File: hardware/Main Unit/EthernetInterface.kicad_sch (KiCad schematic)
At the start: 22 parts, among them J13 HFJ11-2450E-L21RL, U7 KSZ8081RND

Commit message: Main unit: Add USB port for MCU and 3.3VA rail, start on routing
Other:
- moved on the sheet: FB1
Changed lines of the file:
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@@
 	)
 	(junction
+		(at 133.35 33.02)
+		(diameter 0)
+		(color 0 0 0 0)
+	)
+	(junction
 		(at 92.71 48.26)
 		(diameter 0)
@@
 	)
 	(junction
+		(at 200.66 90.17)
+		(diameter 0)
+		(color 0 0 0 0)
+	)
+	(junction
 		(at 165.1 39.37)
 		(diameter 0)
@@
 	(wire
 		(pts
+			(xy 133.35 33.02) (xy 127 33.02)
+		)
+		(stroke
+			(width 0)
+			(type default)
+		)
+	)
+	(wire
+		(pts
 			(xy 139.7 66.04) (xy 170.18 66.04)
 		)
@@
 	(wire
 		(pts
-			(xy 148.59 33.02) (xy 140.97 33.02)
+			(xy 156.21 33.02) (xy 148.59 33.02)
 		)
 		(stroke
@@
 	(wire
 		(pts
-			(xy 200.66 78.74) (xy 200.66 91.44)
+			(xy 200.66 78.74) (xy 200.66 90.17)
 		)
 		(stroke
@@
 	(wire
 		(pts
-			(xy 148.59 30.48) (xy 148.59 33.02)
+			(xy 156.21 30.48) (xy 156.21 33.02)
 		)
 		(stroke
@@
 	(wire
 		(pts
-			(xy 135.89 33.02) (xy 127 33.02)
+			(xy 143.51 33.02) (xy 133.35 33.02)
 		)
 		(stroke
@@
 	(wire
 		(pts
+			(xy 200.66 90.17) (xy 200.66 91.44)
+		)
+		(stroke
+			(width 0)
+			(type default)
+		)
+	)
+	(wire
+		(pts
 			(xy 137.16 87.63) (xy 137.16 85.09)
 		)
@@
 	)
 	(symbol
+		(lib_id "power:PWR_FLAG")
+		(at 133.35 33.02 0)
+		(unit 1)
+		(exclude_from_sim no)
+		(in_bom yes)
+		(on_board yes)
+		(dnp no)
+		(fields_autoplaced yes)
+		(property "Reference" "#FLG02"
+			(at 133.35 31.115 0)
+			(effects
+				(font
+					(size 1.27 1.27)
+				)
+				(hide yes)
+			)
+		)
+		(property "Value" "PWR_FLAG"
+			(at 133.35 27.94 0)
+			(effects
+				(font
+					(size 1.27 1.27)
+				)
+			)
+		)
+		(property "Footprint" ""
+			(at 133.35 33.02 0)
+			(effects
+				(font
+					(size 1.27 1.27)
+				)
+				(hide yes)
+			)
+		)
+		(property "Datasheet" "~"
+			(at 133.35 33.02 0)
+			(effects
+				(font
+					(size 1.27 1.27)
+				)
+				(hide yes)
+			)
+		)
+		(property "Description" "Special symbol for telling ERC where power comes from"
+			(at 133.35 33.02 0)
+			(effects
+				(font
+					(size 1.27 1.27)
+				)
+				(hide yes)
+			)
+		)
+		(pin "1"
+		)
+		(instances
+			(project ""
+				(path "/7d91f165-331a-4c48-9d02-ee2a0aa7e94a/f20a5acb-4894-4073-8c07-952a30c65f74"
+					(reference "#FLG02")
+					(unit 1)
+				)
+			)
+		)
+	)
+	(symbol
 		(lib_id "Device:R_Small_US")
 		(at 81.28 69.85 90)
@@
 	(symbol
 		(lib_id "power:+8V")
-		(at 148.59 30.48 0)
+		(at 156.21 30.48 0)
 		(unit 1)
 		(exclude_from_sim no)
@@
 		(dnp no)
 		(property "Reference" "#PWR0118"
-			(at 148.59 34.29 0)
+			(at 156.21 34.29 0)
 			(effects
 				(font
@@
 		)
 		(property "Value" "+3.3V"
-			(at 152.146 29.718 0)
+			(at 159.766 29.718 0)
 			(effects
 				(font
@@
 		)
 		(property "Footprint" ""
-			(at 148.59 30.48 0)
+			(at 156.21 30.48 0)
 			(effects
 				(font
@@
 		)
 		(property "Datasheet" ""
-			(at 148.59 30.48 0)
+			(at 156.21 30.48 0)
 			(effects
 				(font
@@
 		)
 		(property "Description" "Power symbol creates a global label with name \"+8V\""
-			(at 148.59 30.48 0)
+			(at 156.21 30.48 0)
 			(effects
 				(font
@@
 	(symbol
 		(lib_id "Device:FerriteBead_Small")
-		(at 138.43 33.02 90)
+		(at 146.05 33.02 90)
 		(unit 1)
 		(exclude_from_sim no)
@@
 		(dnp no)
 		(property "Reference" "FB1"
-			(at 140.97 27.94 90)
+			(at 148.59 27.94 90)
 			(effects
 				(font
@@
 		)
 		(property "Value" "300@100MHz"
-			(at 138.43 30.48 90)
+			(at 146.05 30.48 90)
 			(effects
 				(font
@@
 		)
 		(property "Footprint" "Resistor_SMD:R_1206_3216Metric"
-			(at 138.43 34.798 90)
+			(at 146.05 34.798 90)
 			(effects
 				(font
@@
 		)
 		(property "Datasheet" "~"
-			(at 138.43 33.02 0)
+			(at 146.05 33.02 0)
 			(effects
 				(font
@@
 		)
 		(property "Description" "Ferrite bead, small symbol"
-			(at 138.43 33.02 0)
+			(at 146.05 33.02 0)
 			(effects
 				(font
@@
 		)
 		(property "SKU" "732-4654-1-ND"
-			(at 138.43 33.02 0)
+			(at 146.05 33.02 0)
 			(effects
 				(font
@@
 		)
 		(property "Supplier" "Digi-Key"
-			(at 138.43 33.02 0)
+			(at 146.05 33.02 0)
 			(effects
 				(font
@@
 		)
 		(property "LibRef" "742792121"
-			(at 138.43 33.02 0)
+			(at 146.05 33.02 0)
 			(effects
 				(font
@@
 					(unit 1)
 				)
+			)
+		)
+	)
+	(symbol
+		(lib_id "power:PWR_FLAG")
+		(at 200.66 90.17 90)
+		(unit 1)
+		(exclude_from_sim no)
+		(in_bom yes)
+		(on_board yes)
+		(dnp no)
+		(fields_autoplaced yes)
+		(property "Reference" "#FLG03"
+			(at 198.755 90.17 0)
+			(effects
+				(font
+					(size 1.27 1.27)
+				)
+				(hide yes)
+			)
+		)
+		(property "Value" "PWR_FLAG"
+			(at 196.85 90.1699 90)
+			(effects
+				(font
+					(size 1.27 1.27)
+				)
+				(justify left)
+			)
+		)
+		(property "Footprint" ""
+			(at 200.66 90.17 0)
+			(effects
+				(font
+					(size 1.27 1.27)
+				)
+				(hide yes)
+			)
+		)
+		(property "Datasheet" "~"
+			(at 200.66 90.17 0)
+			(effects
+				(font
+					(size 1.27 1.27)
+				)
+				(hide yes)
+			)
+		)
+		(property "Description" "Special symbol for telling ERC where power comes from"
+			(at 200.66 90.17 0)
+			(effects
+				(font
+					(size 1.27 1.27)
+				)
+				(hide yes)
+			)
+		)
+		(pin "1"
+		)
+		(instances
+			(project ""
+				(path "/7d91f165-331a-4c48-9d02-ee2a0aa7e94a/f20a5acb-4894-4073-8c07-952a30c65f74"
+					(reference "#FLG03")
+					(unit 1)
+				)

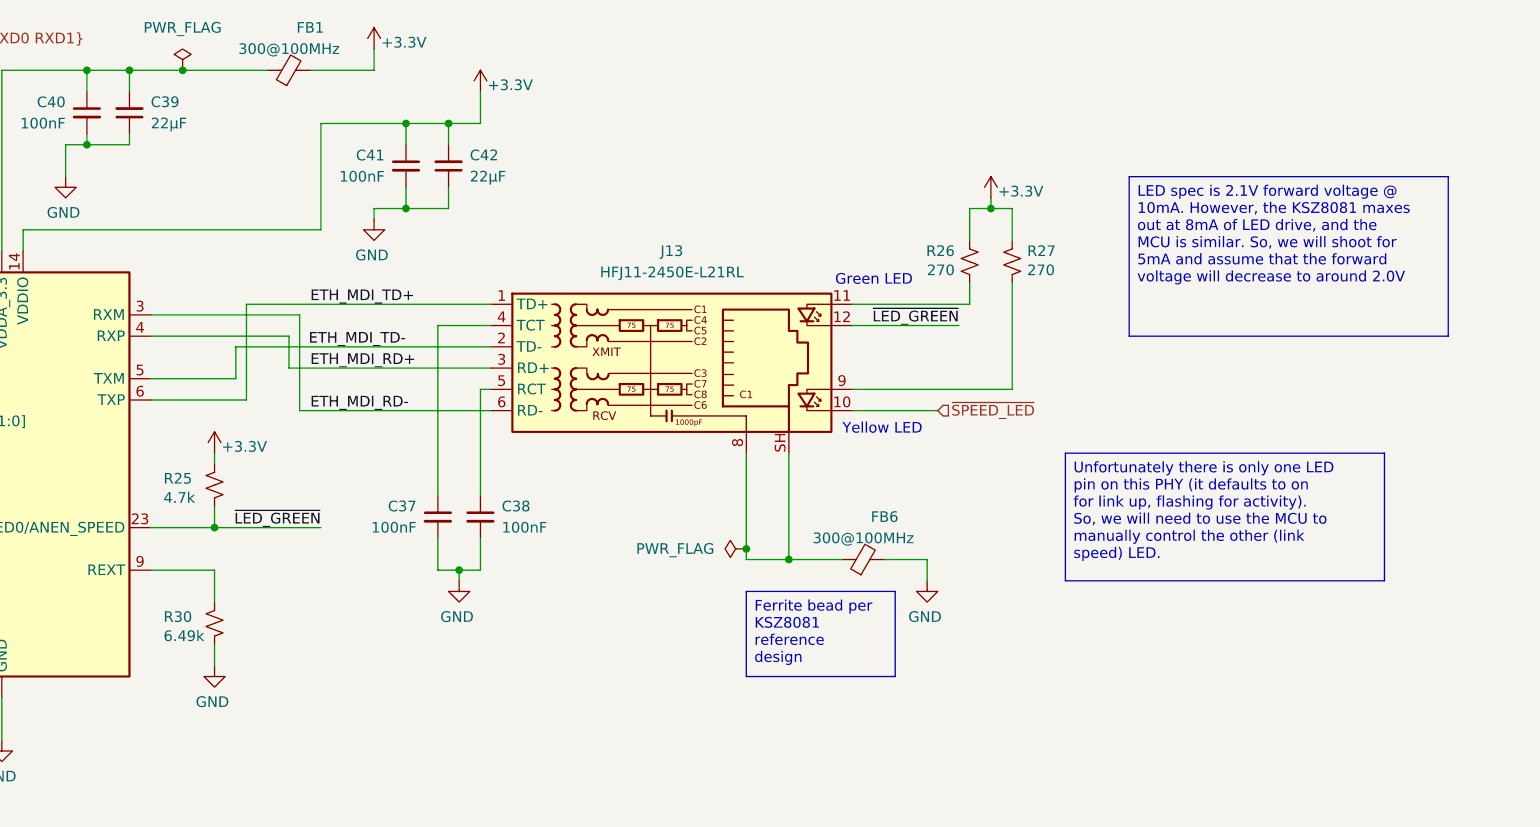
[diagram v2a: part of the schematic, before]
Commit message: Route most of the data lines on the PCB
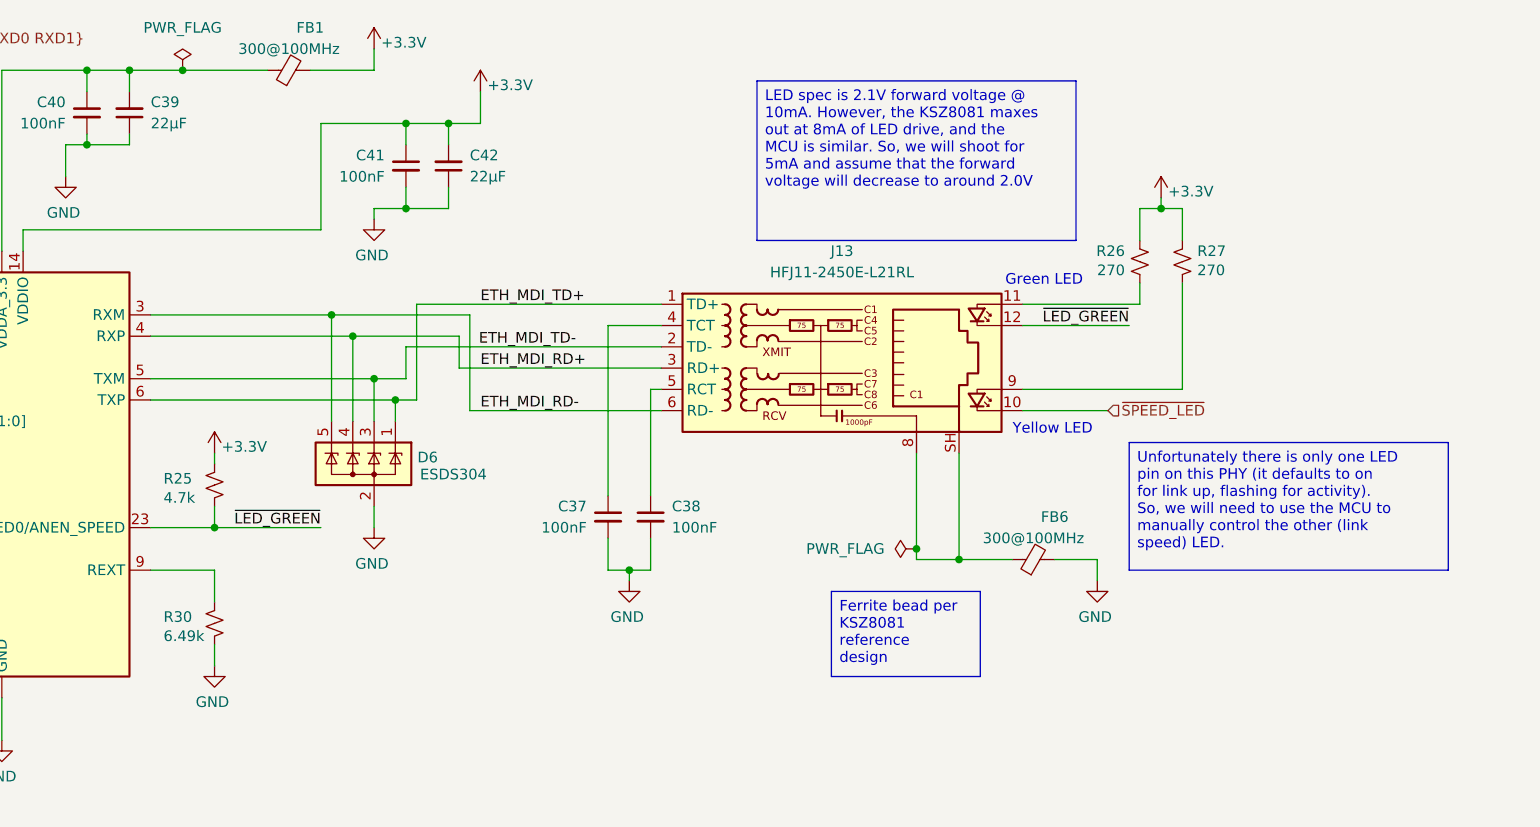
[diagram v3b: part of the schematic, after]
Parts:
- added D6: ESDS304, Package_TO_SOT_SMD:SOT-23-5, symbol Power_Protection:ESDS304
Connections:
- net ETH_MDI_RD+: now also D6.4 (K)
- net ETH_MDI_RD-: now also D6.5 (K)
- net ETH_MDI_TD+: now also D6.1 (K)
- net ETH_MDI_TD-: now also D6.3 (K)
- net GND: now also D6.2 (A)
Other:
- moved on the sheet: C37, C38, FB6, J13, R26, R27

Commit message: Add LEDs and 5V regulator to main unit
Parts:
- J13: footprint Project Library:RJ45_HALO_HFJ11-x2450E-LxxRL_Horizontal-Fixed3DModel -> Connector_RJ:RJ45_HALO_HFJ11-x2450E-LxxRL_Horizontal
- U7: footprint Project Library:QFN-24-1EP_4x4mm_P0.5mm_EP2.65x2.65mm-LengthenedPads -> Package_DFN_QFN:QFN-24-1EP_4x4mm_P0.5mm_EP2.6x2.6mm
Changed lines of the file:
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@@
 		)
 		(instances
-			(project "Main Unit"
+			(project "HackerDAQ Main Unit"
 				(path "/7d91f165-331a-4c48-9d02-ee2a0aa7e94a/f20a5acb-4894-4073-8c07-952a30c65f74"
 					(reference "#PWR0145")
@@
 		)
 		(instances
-			(project ""
+			(project "HackerDAQ Main Unit"
 				(path "/7d91f165-331a-4c48-9d02-ee2a0aa7e94a/f20a5acb-4894-4073-8c07-952a30c65f74"
 					(reference "#FLG02")
@@
 			)
 		)
-		(property "Description" "Resistor 33 ohm 1% 0.1W 0603"
+		(property "Description" "Resistor, small US symbol"
 			(at 81.28 69.85 0)
 			(effects
@@
 		)
 		(instances
-			(project "Main Unit"
+			(project "HackerDAQ Main Unit"
 				(path "/7d91f165-331a-4c48-9d02-ee2a0aa7e94a/f20a5acb-4894-4073-8c07-952a30c65f74"
 					(reference "R13")
@@
 		)
 		(instances
-			(project "Main Unit"
+			(project "HackerDAQ Main Unit"
 				(path "/7d91f165-331a-4c48-9d02-ee2a0aa7e94a/f20a5acb-4894-4073-8c07-952a30c65f74"
 					(reference "#PWR089")
@@
 			)
 		)
-		(property "Description" "CAP CER 22uF 16V X7R 1210"
+		(property "Description" "Unpolarized capacitor, small symbol"
 			(at 127 38.1 0)
 			(effects
@@
 		)
 		(instances
-			(project "Main Unit"
+			(project "HackerDAQ Main Unit"
 				(path "/7d91f165-331a-4c48-9d02-ee2a0aa7e94a/f20a5acb-4894-4073-8c07-952a30c65f74"
 					(reference "C39")
@@
 		)
 		(instances
-			(project "Main Unit"
+			(project "HackerDAQ Main Unit"
 				(path "/7d91f165-331a-4c48-9d02-ee2a0aa7e94a/f20a5acb-4894-4073-8c07-952a30c65f74"
 					(reference "C38")
@@
 			)
 		)
-		(property "Description" "CAP CER 22uF 16V X7R 1210"
+		(property "Description" "Unpolarized capacitor, small symbol"
 			(at 165.1 44.45 0)
 			(effects
@@
 		)
 		(instances
-			(project "Main Unit"
+			(project "HackerDAQ Main Unit"
 				(path "/7d91f165-331a-4c48-9d02-ee2a0aa7e94a/f20a5acb-4894-4073-8c07-952a30c65f74"
 					(reference "C42")
@@
 			)
 		)
-		(property "Description" "Resistor 6.49 kOhm 1% 0.1W 0603"
+		(property "Description" "Resistor, small US symbol"
 			(at 137.16 99.06 0)
 			(effects
@@
 		)
 		(instances
-			(project "Main Unit"
+			(project "HackerDAQ Main Unit"
 				(path "/7d91f165-331a-4c48-9d02-ee2a0aa7e94a/f20a5acb-4894-4073-8c07-952a30c65f74"
 					(reference "R30")
@@
 		)
 		(instances
-			(project "Main Unit"
+			(project "HackerDAQ Main Unit"
 				(path "/7d91f165-331a-4c48-9d02-ee2a0aa7e94a/f20a5acb-4894-4073-8c07-952a30c65f74"
 					(reference "C37")
@@
 		)
 		(instances
-			(project "Main Unit"
+			(project "HackerDAQ Main Unit"
 				(path "/7d91f165-331a-4c48-9d02-ee2a0aa7e94a/f20a5acb-4894-4073-8c07-952a30c65f74"
 					(reference "#PWR0118")
@@
 			)
 		)
-		(property "Footprint" "Project Library:QFN-24-1EP_4x4mm_P0.5mm_EP2.65x2.65mm-LengthenedPads"
+		(property "Footprint" "Package_DFN_QFN:QFN-24-1EP_4x4mm_P0.5mm_EP2.6x2.6mm"
 			(at 147.32 107.95 0)
 			(effects
@@
 		)
 		(instances
-			(project ""
+			(project "HackerDAQ Main Unit"
 				(path "/7d91f165-331a-4c48-9d02-ee2a0aa7e94a/f20a5acb-4894-4073-8c07-952a30c65f74"
 					(reference "U7")
@@
 		)
 		(instances
-			(project "Main Unit"
+			(project "HackerDAQ Main Unit"
 				(path "/7d91f165-331a-4c48-9d02-ee2a0aa7e94a/f20a5acb-4894-4073-8c07-952a30c65f74"
 					(reference "C40")
@@
 		)
 		(instances
-			(project "Main Unit"
+			(project "HackerDAQ Main Unit"
 				(path "/7d91f165-331a-4c48-9d02-ee2a0aa7e94a/f20a5acb-4894-4073-8c07-952a30c65f74"
 					(reference "#PWR0116")
@@
 		)
 		(instances
-			(project "Main Unit"
+			(project "HackerDAQ Main Unit"
 				(path "/7d91f165-331a-4c48-9d02-ee2a0aa7e94a/f20a5acb-4894-4073-8c07-952a30c65f74"
 					(reference "#PWR088")
@@
 		)
 		(instances
-			(project "Main Unit"
+			(project "HackerDAQ Main Unit"
 				(path "/7d91f165-331a-4c48-9d02-ee2a0aa7e94a/f20a5acb-4894-4073-8c07-952a30c65f74"
 					(reference "FB1")
@@
 		)
 		(instances
-			(project "Main Unit"
+			(project "HackerDAQ Main Unit"
 				(path "/7d91f165-331a-4c48-9d02-ee2a0aa7e94a/f20a5acb-4894-4073-8c07-952a30c65f74"
 					(reference "C35")
@@
 		)
 		(instances
-			(project ""
+			(project "HackerDAQ Main Unit"
 				(path "/7d91f165-331a-4c48-9d02-ee2a0aa7e94a/f20a5acb-4894-4073-8c07-952a30c65f74"
 					(reference "D6")
@@
 		)
 		(instances
-			(project "Main Unit"
+			(project "HackerDAQ Main Unit"
 				(path "/7d91f165-331a-4c48-9d02-ee2a0aa7e94a/f20a5acb-4894-4073-8c07-952a30c65f74"
 					(reference "C41")
@@
 		)
 		(instances
-			(project "Main Unit"
+			(project "HackerDAQ Main Unit"
 				(path "/7d91f165-331a-4c48-9d02-ee2a0aa7e94a/f20a5acb-4894-4073-8c07-952a30c65f74"
 					(reference "#PWR0114")
@@
 			)
 		)
-		(property "Description" "Resistor 33 ohm 1% 0.1W 0603"
+		(property "Description" "Resistor, small US symbol"
 			(at 81.28 74.93 0)
 			(effects
@@
 		)
 		(instances
-			(project "Main Unit"
+			(project "HackerDAQ Main Unit"
 				(path "/7d91f165-331a-4c48-9d02-ee2a0aa7e94a/f20a5acb-4894-4073-8c07-952a30c65f74"
 					(reference "R16")
@@
 			)
 		)
-		(property "Description" "Resistor 33 ohm 1% 0.1W 0603"
+		(property "Description" "Resistor, small US symbol"
 			(at 72.39 80.01 0)
 			(effects
@@
 		)
 		(instances
-			(project "Main Unit"
+			(project "HackerDAQ Main Unit"
 				(path "/7d91f165-331a-4c48-9d02-ee2a0aa7e94a/f20a5acb-4894-4073-8c07-952a30c65f74"
 					(reference "R17")
@@
 		)
 		(instances
-			(project ""
+			(project "HackerDAQ Main Unit"
 				(path "/7d91f165-331a-4c48-9d02-ee2a0aa7e94a/f20a5acb-4894-4073-8c07-952a30c65f74"
 					(reference "#FLG03")
@@
 		)
 		(instances
-			(project "Main Unit"
+			(project "HackerDAQ Main Unit"
 				(path "/7d91f165-331a-4c48-9d02-ee2a0aa7e94a/f20a5acb-4894-4073-8c07-952a30c65f74"
 					(reference "#PWR0112")
@@
 			)
 		)
-		(property "Description" "Resistor 270 ohm 1% 0.1W 0603"
+		(property "Description" "Resistor, small US symbol"
 			(at 247.65 55.88 0)
 			(effects
@@
 		)
 		(instances
-			(project "Main Unit"
+			(project "HackerDAQ Main Unit"
 				(path "/7d91f165-331a-4c48-9d02-ee2a0aa7e94a/f20a5acb-4894-4073-8c07-952a30c65f74"
 					(reference "R26")
@@
 		)
 		(instances
-			(project "Main Unit"
+			(project "HackerDAQ Main Unit"
 				(path "/7d91f165-331a-4c48-9d02-ee2a0aa7e94a/f20a5acb-4894-4073-8c07-952a30c65f74"
 					(reference "#PWR0120")
@@
 			)
 		)
-		(property "Description" "Resistor 33 ohm 1% 0.1W 0603"
+		(property "Description" "Resistor, small US symbol"
 			(at 72.39 72.39 0)
 			(effects
@@
 		)
 		(instances
-			(project "Main Unit"
+			(project "HackerDAQ Main Unit"
 				(path "/7d91f165-331a-4c48-9d02-ee2a0aa7e94a/f20a5acb-4894-4073-8c07-952a30c65f74"
 					(reference "R14")
@@
 		)
 		(instances
-			(project "Main Unit"
+			(project "HackerDAQ Main Unit"
 				(path "/7d91f165-331a-4c48-9d02-ee2a0aa7e94a/f20a5acb-4894-4073-8c07-952a30c65f74"
 					(reference "R28")
@@
 		)
 		(instances
-			(project "Main Unit"
+			(project "HackerDAQ Main Unit"
 				(path "/7d91f165-331a-4c48-9d02-ee2a0aa7e94a/f20a5acb-4894-4073-8c07-952a30c65f74"
 					(reference "#PWR0115")
@@
 		)
 		(instances
-			(project "Main Unit"
+			(project "HackerDAQ Main Unit"
 				(path "/7d91f165-331a-4c48-9d02-ee2a0aa7e94a/f20a5acb-4894-4073-8c07-952a30c65f74"
 					(reference "FB6")
@@
 		)
 		(instances
-			(project "Main Unit"
+			(project "HackerDAQ Main Unit"
 				(path "/7d91f165-331a-4c48-9d02-ee2a0aa7e94a/f20a5acb-4894-4073-8c07-952a30c65f74"
 					(reference "#PWR0119")
@@
 		)
 		(instances
-			(project "Main Unit"
+			(project "HackerDAQ Main Unit"
 				(path "/7d91f165-331a-4c48-9d02-ee2a0aa7e94a/f20a5acb-4894-4073-8c07-952a30c65f74"
 					(reference "#PWR0113")
@@
 		)
 		(instances
-			(project "Main Unit"
+			(project "HackerDAQ Main Unit"
 				(path "/7d91f165-331a-4c48-9d02-ee2a0aa7e94a/f20a5acb-4894-4073-8c07-952a30c65f74"
 					(reference "R29")
@@
 			)
 		)
-		(property "Footprint" "Project Library:RJ45_HALO_HFJ11-x2450E-LxxRL_Horizontal-Fixed3DModel"
+		(property "Footprint" "Connector_RJ:RJ45_HALO_HFJ11-x2450E-LxxRL_Horizontal"
 			(at 210.82 56.515 0)
 			(effects
@@
 		)
 		(instances
-			(project ""
+			(project "HackerDAQ Main Unit"
 				(path "/7d91f165-331a-4c48-9d02-ee2a0aa7e94a/f20a5acb-4894-4073-8c07-952a30c65f74"
 					(reference "J13")
@@
 			)
 		)
-		(property "Description" "Resistor 270 ohm 1% 0.1W 0603"
+		(property "Description" "Resistor, small US symbol"
 			(at 252.73 55.88 0)
 			(effects
@@
 		)
 		(instances
-			(project "Main Unit"
+			(project "HackerDAQ Main Unit"
 				(path "/7d91f165-331a-4c48-9d02-ee2a0aa7e94a/f20a5acb-4894-4073-8c07-952a30c65f74"
 					(reference "R27")
@@
 		)
 		(instances
-			(project "Main Unit"
+			(project "HackerDAQ Main Unit"
 				(path "/7d91f165-331a-4c48-9d02-ee2a0aa7e94a/f20a5acb-4894-4073-8c07-952a30c65f74"
 					(reference "#PWR0111")
@@
 			)
 		)
-		(property "Description" "Resistor 4.7 kOhm 1% 0.1W 0603"
+		(property "Description" "Resistor, small US symbol"
 			(at 137.16 82.55 0)
 			(effects
@@
 		)
 		(instances
-			(project "Main Unit"
+			(project "HackerDAQ Main Unit"
 				(path "/7d91f165-331a-4c48-9d02-ee2a0aa7e94a/f20a5acb-4894-4073-8c07-952a30c65f74"
 					(reference "R25")
@@
 		)
 		(instances
-			(project "Main Unit"
+			(project "HackerDAQ Main Unit"
 				(path "/7d91f165-331a-4c48-9d02-ee2a0aa7e94a/f20a5acb-4894-4073-8c07-952a30c65f74"
 					(reference "#PWR0117")
@@
 		)
 		(instances
-			(project "Main Unit"
+			(project "HackerDAQ Main Unit"
 				(path "/7d91f165-331a-4c48-9d02-ee2a0aa7e94a/f20a5acb-4894-4073-8c07-952a30c65f74"
 					(reference "C36")
@@
 		)
 		(instances
-			(project "Main Unit"
+			(project "HackerDAQ Main Unit"
 				(path "/7d91f165-331a-4c48-9d02-ee2a0aa7e94a/f20a5acb-4894-4073-8c07-952a30c65f74"
 					(reference "#PWR0121")

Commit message: Main board routed!!
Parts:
- J13: footprint Connector_RJ:RJ45_HALO_HFJ11-x2450E-LxxRL_Horizontal -> Project Library:RJ45_HALO_HFJ11-x2450E-LxxRL_Horizontal-Fixed3DModel
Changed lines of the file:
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@@
 			)
 		)
-		(property "Footprint" "Connector_RJ:RJ45_HALO_HFJ11-x2450E-LxxRL_Horizontal"
+		(property "Footprint" "Project Library:RJ45_HALO_HFJ11-x2450E-LxxRL_Horizontal-Fixed3DModel"
 			(at 210.82 56.515 0)
 			(effects
